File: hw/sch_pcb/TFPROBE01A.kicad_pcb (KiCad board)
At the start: 2 copper layers, 14 x 10 mm, 8 parts, among them J1 HEADER_1x03, M3 HOLE, M4 HOLE, U1 AH3572, U2 VCNT2020

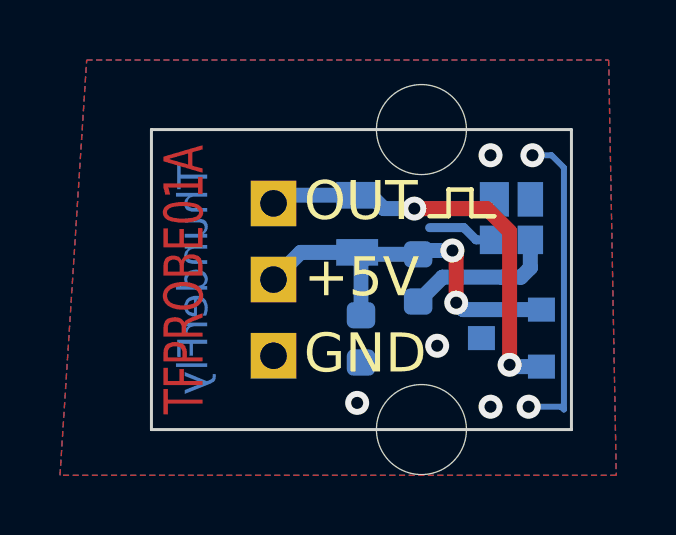
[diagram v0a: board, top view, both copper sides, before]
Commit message: Flip pin-header connector to opposite side. #3
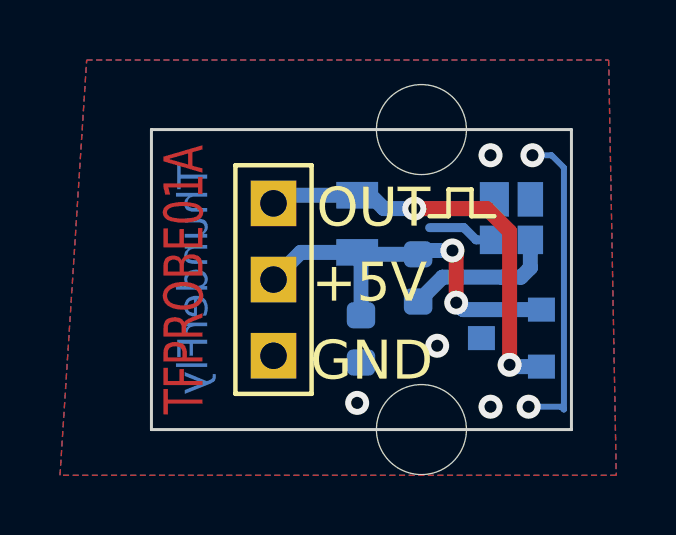
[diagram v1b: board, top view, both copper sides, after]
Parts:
- J1: moved to F.Cu
- turned J1 to 0 degrees
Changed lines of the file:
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@@
-(kicad_pcb (version 20201002) (generator pcbnew)
+(kicad_pcb (version 20201116) (generator pcbnew)
   (general
     (thickness 1.6)
@@
   (net 3 "/COUNT")
   (net 4 "Net-(R1-Pad2)")
-  (module "Mlab_Mechanical:dira_3mm" (layer "F.Cu")
+  (footprint "Mlab_Mechanical:dira_3mm" (layer "F.Cu")
     (at 8.89 -10.033)
     (property "Sheet file" "C:/Chroust/stare/TF_G/OPTMAGPROBE01/hw/sch_pcb/OPTMAGPROBE01A.kicad_sch")
@@
     (pad "" np_thru_hole circle (at 0.11 0.033) (size 3 3) (drill 3) (layers *.Mask))
   )
-  (module "Mlab_Mechanical:dira_3mm" (layer "F.Cu")
+  (footprint "Mlab_Mechanical:dira_3mm" (layer "F.Cu")
     (at 9 0)
     (property "Sheet file" "C:/Chroust/stare/TF_G/OPTMAGPROBE01/hw/sch_pcb/OPTMAGPROBE01A.kicad_sch")
@@
     (pad "" np_thru_hole circle (at 0 0) (size 3 3) (drill 3) (layers *.Mask))
   )
-  (module "Mlab_R:SMD-0603" (layer "B.Cu")
+  (footprint "Mlab_Pin_Headers:Straight_1x03" locked (layer "F.Cu")
+    (at 4.069 -5)
+    (descr "pin header straight 1x03")
+    (tags "pin header straight 1x03")
+    (property "Sheet file" "C:/Chroust/stare/TF_G/OPTMAGPROBE01/hw/sch_pcb/OPTMAGPROBE01A.kicad_sch")
+    (property "Sheet name" "")
+    (attr through_hole)
+    (fp_text reference "J1" (at 0 -5.08 180) (layer "F.SilkS") hide
+      (effects (font (size 1.5 1.5) (thickness 0.15)))
+    )
+    (fp_text value "HEADER_1x03" (at 0 5.08 180) (layer "F.SilkS") hide
+      (effects (font (size 1.5 1.5) (thickness 0.15)))
+    )
+    (fp_line (start 1.27 3.81) (end -1.27 3.81) (layer "F.SilkS") (width 0.15))
+    (fp_line (start 1.27 -3.81) (end 1.27 3.81) (layer "F.SilkS") (width 0.15))
+    (fp_line (start -1.27 -3.81) (end 1.27 -3.81) (layer "F.SilkS") (width 0.15))
+    (fp_line (start -1.27 3.81) (end -1.27 -3.81) (layer "F.SilkS") (width 0.15))
+    (fp_line (start -1.27 3.81) (end -1.27 -3.81) (layer "F.Fab") (width 0.15))
+    (fp_line (start 1.27 3.81) (end -1.27 3.81) (layer "F.Fab") (width 0.15))
+    (fp_line (start 1.27 -3.81) (end 1.27 3.81) (layer "F.Fab") (width 0.15))
+    (fp_line (start -1.27 -3.81) (end 1.27 -3.81) (layer "F.Fab") (width 0.15))
+    (pad "1" thru_hole rect (at 0 -2.54) (size 1.524 1.524) (drill 0.889) (layers *.Cu *.Mask)
+      (net 3 "/COUNT"))
+    (pad "2" thru_hole rect (at 0 0) (size 1.524 1.524) (drill 0.889) (layers *.Cu *.Mask)
+      (net 1 "+5V"))
+    (pad "3" thru_hole rect (at 0 2.54) (size 1.524 1.524) (drill 0.889) (layers *.Cu *.Mask)
+      (net 2 "GND"))
+    (model "${KISYS3DMOD}/Connector_PinHeader_2.54mm.3dshapes/PinHeader_1x03_P2.54mm_Vertical.wrl"
+      (offset (xyz 0 2.54 0))
+      (scale (xyz 1 1 1))
+      (rotate (xyz 0 0 0))
+    )
+  )
+  (footprint "Mlab_R:SMD-0603" (layer "B.Cu")
     (at 8.89 -5.0545 -90)
     (descr "Resistor SMD 0603 (1608 Metric), square (rectangular) end terminal, IPC_7351 nominal, (Body size source: http://www.tortai-tech.com/upload/download/2011102023233369053.pdf), generated with kicad-footprint-generator")
@@
     )
   )
-  (module "Package_TO_SOT_SMD:SOT-23" (layer "B.Cu")
+  (footprint "Package_TO_SOT_SMD:SOT-23" (layer "B.Cu")
     (at 12 -3.048 180)
     (descr "SOT-23, Standard")
@@
     )
   )
-  (module "Mlab_R:SMD-0603" (layer "B.Cu")
+  (footprint "Mlab_R:SMD-0603" (layer "B.Cu")
     (at 6.985 -3.0225 -90)
     (descr "Resistor SMD 0603 (1608 Metric), square (rectangular) end terminal, IPC_7351 nominal, (Body size source: http://www.tortai-tech.com/upload/download/2011102023233369053.pdf), generated with kicad-footprint-generator")
@@
     )
   )
-  (module "Mlab_R:SMD-0805" (layer "B.Cu")
+  (footprint "Mlab_R:SMD-0805" (layer "B.Cu")
     (at 6.858 -6.858 90)
     (property "Sheet file" "C:/Chroust/stare/TF_G/OPTMAGPROBE01/hw/sch_pcb/OPTMAGPROBE01A.kicad_sch")
@@
     )
   )
-  (module "Mlab_IO:XDCR_VCNT2020" (layer "B.Cu")
+  (footprint "Mlab_IO:XDCR_VCNT2020" (layer "B.Cu")
     (at 12 -7.048)
     (property "Field4" "Vishay")
@@
     (fp_line (start -1.37 1) (end -1.37 -1) (layer "B.SilkS") (width 0.127))
     (fp_line (start 1.37 1) (end 1.37 -1) (layer "B.SilkS") (width 0.127))
-    (fp_circle (center -1.91352 0.769763) (end -1.81352 0.769763) (layer "B.SilkS") (width 0.2))
+    (fp_circle (center -1.91352 0.769763) (end -1.81352 0.769763) (layer "B.SilkS") (width 0.2) (fill none))
     (fp_line (start 1.5 1.45) (end 1.5 -1.45) (layer "B.CrtYd") (width 0.05))
     (fp_line (start 1.5 1.45) (end -1.5 1.45) (layer "B.CrtYd") (width 0.05))
@@
     (fp_line (start 1.25 1) (end -1.25 1) (layer "B.Fab") (width 0.127))
     (fp_line (start 1.25 1) (end 1.25 -1) (layer "B.Fab") (width 0.127))
-    (fp_circle (center -1.91352 0.769763) (end -1.81352 0.769763) (layer "B.Fab") (width 0.2))
+    (fp_circle (center -1.91352 0.769763) (end -1.81352 0.769763) (layer "B.Fab") (width 0.2) (fill none))
     (pad "1" smd rect (at -0.57 0.725) (size 0.97 0.95) (layers "B.Cu" "B.Paste" "B.Mask")
       (net 2 "GND"))
@@
     )
   )
-  (module "Mlab_Pin_Headers:Straight_1x03" locked (layer "B.Cu")
-    (at 4.069 -5 180)
-    (descr "pin header straight 1x03")
-    (tags "pin header straight 1x03")
-    (property "Sheet file" "C:/Chroust/stare/TF_G/OPTMAGPROBE01/hw/sch_pcb/OPTMAGPROBE01A.kicad_sch")
-    (property "Sheet name" "")
-    (attr through_hole)
-    (fp_text reference "J1" (at 0 5.08 180) (layer "B.SilkS") hide
-      (effects (font (size 1.5 1.5) (thickness 0.15)) (justify mirror))
-    )
-    (fp_text value "HEADER_1x03" (at 0 -5.08 180) (layer "B.SilkS") hide
-      (effects (font (size 1.5 1.5) (thickness 0.15)) (justify mirror))
-    )
-    (fp_text user "1" (at -1.651 2.54 180) (layer "B.SilkS")
-      (effects (font (size 0.5 0.5) (thickness 0.05)) (justify mirror))
-    )
-    (fp_line (start 1.27 -3.81) (end -1.27 -3.81) (layer "B.SilkS") (width 0.15))
-    (fp_line (start 1.27 3.81) (end 1.27 -3.81) (layer "B.SilkS") (width 0.15))
-    (fp_line (start -1.27 3.81) (end 1.27 3.81) (layer "B.SilkS") (width 0.15))
-    (fp_line (start -1.27 -3.81) (end -1.27 3.81) (layer "B.SilkS") (width 0.15))
-    (fp_line (start -1.27 -3.81) (end -1.27 3.81) (layer "B.Fab") (width 0.15))
-    (fp_line (start 1.27 -3.81) (end -1.27 -3.81) (layer "B.Fab") (width 0.15))
-    (fp_line (start 1.27 3.81) (end 1.27 -3.81) (layer "B.Fab") (width 0.15))
-    (fp_line (start -1.27 3.81) (end 1.27 3.81) (layer "B.Fab") (width 0.15))
-    (pad "1" thru_hole rect (at 0 2.54 180) (size 1.524 1.524) (drill 0.889) (layers *.Cu *.Mask)
-      (net 3 "/COUNT"))
-    (pad "2" thru_hole rect (at 0 0 180) (size 1.524 1.524) (drill 0.889) (layers *.Cu *.Mask)
-      (net 1 "+5V"))
-    (pad "3" thru_hole rect (at 0 -2.54 180) (size 1.524 1.524) (drill 0.889) (layers *.Cu *.Mask)
-      (net 2 "GND"))
-    (model "${KISYS3DMOD}/Connector_PinHeader_2.54mm.3dshapes/PinHeader_1x03_P2.54mm_Vertical.wrl"
-      (offset (xyz 0 2.54 0))
-      (scale (xyz 1 1 1))
-      (rotate (xyz 0 0 0))
-    )
-  )
   (gr_line (start 9.906 -8.001) (end 10.668 -8.001) (layer "F.SilkS") (width 0.15))
   (gr_line (start 9.271 -7.112) (end 9.906 -7.112) (layer "F.SilkS") (width 0.15))
@@
   (gr_line (start 9.906 -7.112) (end 9.906 -8.001) (layer "F.SilkS") (width 0.15))
   (gr_line (start 10.668 -7.112) (end 11.43 -7.112) (layer "F.SilkS") (width 0.15))
-  (gr_rect (start 0 0) (end 14 -10) (layer "Edge.Cuts") (width 0.1))
+  (gr_rect (start 0 0) (end 14 -10) (layer "Edge.Cuts") (width 0.1) (fill none))
   (gr_text "TFPROBE01A" (at 1.1 -5 90) (layer "F.Cu")
     (effects (font (size 1.3 1) (thickness 0.15)))
@@
     (effects (font (size 1 1) (thickness 0.15)) (justify mirror))
   )
-  (gr_text "GND" (at 5.08 -2.54) (layer "F.SilkS")
+  (gr_text "GND" (at 5.3 -2.3) (layer "F.SilkS")
     (effects (font (size 1.3 1.3) (thickness 0.2)) (justify left))
   )
-  (gr_text "OUT" (at 5.08 -7.62) (layer "F.SilkS")
+  (gr_text "OUT" (at 5.5 -7.4) (layer "F.SilkS")
     (effects (font (size 1.3 1.3) (thickness 0.2)) (justify left))
   )
-  (gr_text "+5V" (at 5.08 -5.08) (layer "F.SilkS")
+  (gr_text "+5V" (at 5.339 -4.9) (layer "F.SilkS")
     (effects (font (size 1.3 1.3) (thickness 0.2)) (justify left))
   )
@@
     (style (thickness 0.15) (arrow_length 1.27) (text_position_mode 0) (extension_height 0.58642) (extension_offset 0.5) keep_text_aligned)
   )
+  (dimension (type aligned) (layer "Cmts.User")
+    (pts (xy 2.799 -1.19) (xy 2.799 -8.81))
+    (height -4.099)
+    (gr_text "7,6200 mm" (at -2.45 -5 90) (layer "Cmts.User")
+      (effects (font (size 1 1) (thickness 0.15)))
+    )
+    (format (units 3) (units_format 1) (precision 4))
+    (style (thickness 0.15) (arrow_length 1.27) (text_position_mode 0) (extension_height 0.58642) (extension_offset 0.5) keep_text_aligned)
+  )
